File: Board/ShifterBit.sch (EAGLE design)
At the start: 14 parts, among them P1 PINHD-1X10, P2 PINHD-1X10

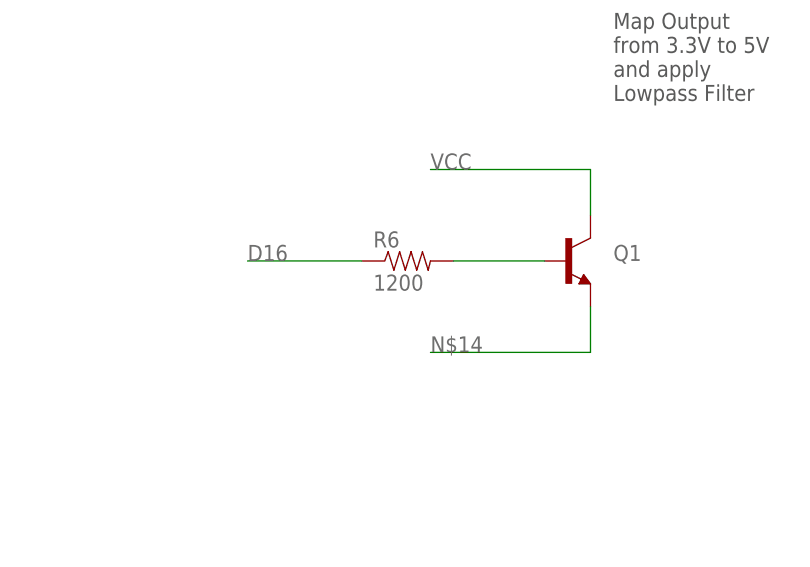
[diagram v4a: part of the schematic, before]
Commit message: changed resistor name
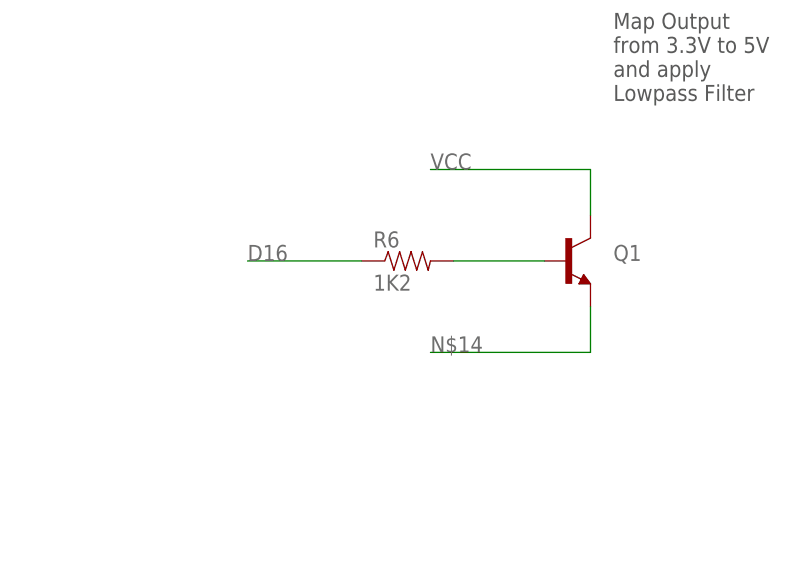
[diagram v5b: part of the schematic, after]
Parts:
- R6: value 1200 -> 1K2
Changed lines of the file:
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@@
 <part name="R5" library="SparkFun-Passives" deviceset="RESISTOR" device="0603-RES" value="560"/>
 <part name="Q1" library="SparkFun-DiscreteSemi" deviceset="TRANSISTOR_NPN" device="BC547"/>
-<part name="R6" library="SparkFun-Resistors" deviceset="RESISTOR" device="0603" value="1200"/>
+<part name="R6" library="SparkFun-Resistors" deviceset="RESISTOR" device="0603" value="1K2"/>
 </parts>
 <sheets>

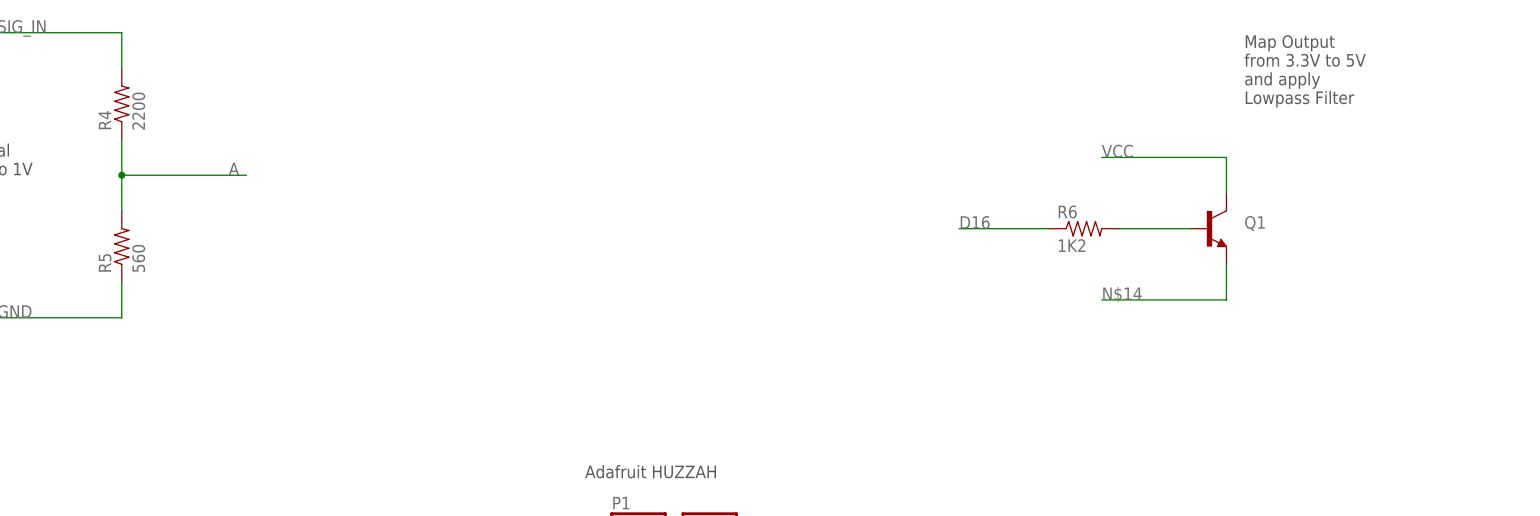
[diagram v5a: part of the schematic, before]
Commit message: added component to board
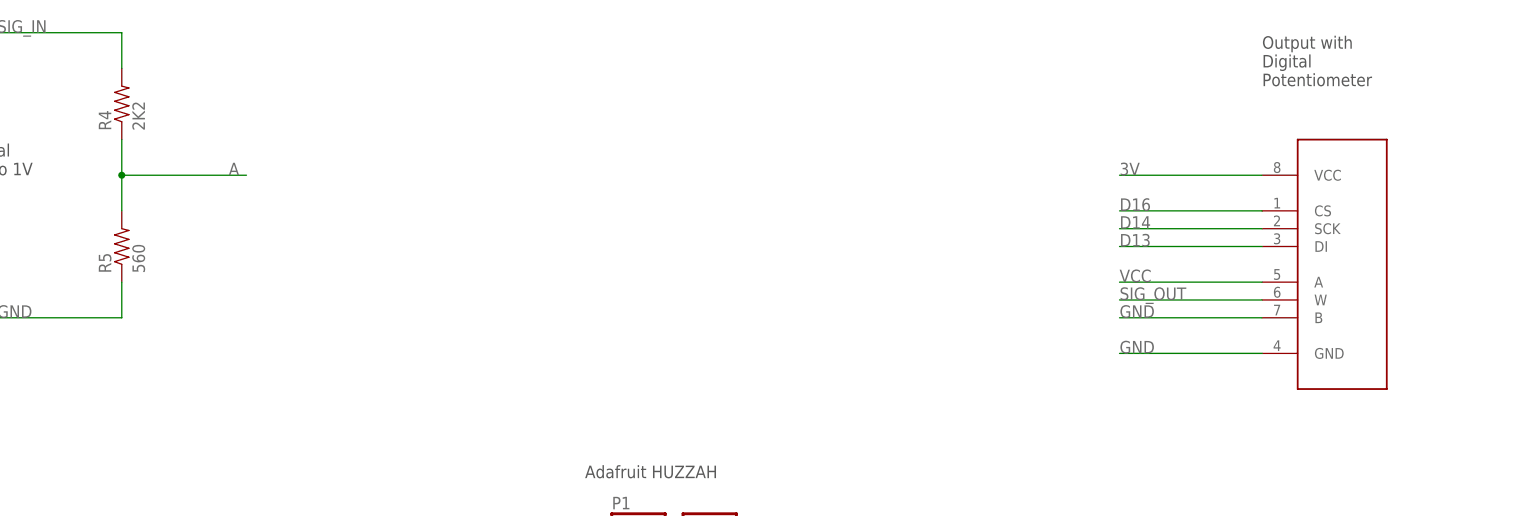
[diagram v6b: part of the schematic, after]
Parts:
- removed Q1: (no value), SparkFun-DiscreteSemi:TRANSISTOR_NPNBC547
- removed R6: 1K2, SparkFun-Resistors:RESISTOR0603
- added DPOT1: MCP41XXX, SparkFun-AnalogIC:MCP41XXX
- R4: value 2200 -> 2K2
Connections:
- removed net N$10: Q1.B, R6.2
- removed net N$14: Q1.E
- net 3V: now also DPOT1.VCC
- net D13: now also DPOT1.DI
- net D14: now also DPOT1.SCK
- net D16: now also DPOT1.CS; no longer R6.1
- net GND: now also DPOT1.B, DPOT1.GND
- net SIG_OUT: now also DPOT1.W
- net VCC: now also DPOT1.A; no longer Q1.C
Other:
- note added: "Output with Digital Potentiometer"
- note removed: "Map Output from 3.3V to 5V and apply Lowpass Filter"
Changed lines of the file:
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@@
 <layer number="56" name="wert" color="7" fill="1" visible="no" active="no"/>
 <layer number="57" name="tCAD" color="7" fill="1" visible="no" active="no"/>
+<layer number="59" name="tCarbon" color="7" fill="1" visible="no" active="no"/>
+<layer number="60" name="bCarbon" color="7" fill="1" visible="no" active="no"/>
 <layer number="90" name="Modules" color="5" fill="1" visible="yes" active="yes"/>
 <layer number="91" name="Nets" color="2" fill="1" visible="yes" active="yes"/>
@@
 <layer number="127" name="_tValues" color="7" fill="1" visible="yes" active="yes"/>
 <layer number="128" name="_bValues" color="7" fill="1" visible="yes" active="yes"/>
+<layer number="129" name="Mask" color="7" fill="1" visible="yes" active="yes"/>
 <layer number="131" name="tAdjust" color="7" fill="1" visible="yes" active="yes"/>
 <layer number="132" name="bAdjust" color="7" fill="1" visible="yes" active="yes"/>
@@
 <part name="R2" library="SparkFun-Passives" deviceset="RESISTOR" device="0603-RES" value="56"/>
 <part name="R3" library="SparkFun-Passives" deviceset="RESISTOR" device="0603-RES" value="56"/>
-<part name="R4" library="SparkFun-Passives" deviceset="RESISTOR" device="0603-RES" value="2200"/>
+<part name="R4" library="SparkFun-Passives" deviceset="RESISTOR" device="0603-RES" value="2K2"/>
 <part name="R5" library="SparkFun-Passives" deviceset="RESISTOR" device="0603-RES" value="560"/>
-<part name="Q1" library="SparkFun-DiscreteSemi" deviceset="TRANSISTOR_NPN" device="BC547"/>
-<part name="R6" library="SparkFun-Resistors" deviceset="RESISTOR" device="0603" value="1K2"/>
+<part name="DPOT1" library="SparkFun-AnalogIC" deviceset="MCP41XXX" device="" value="MCP41XXX"/>
 </parts>
 <sheets>
@@
 <text x="20.32" y="76.2" size="1.778" layer="97">Input</text>
 <text x="205.74" y="73.66" size="1.778" layer="97">Output</text>
-<text x="193.04" y="185.42" size="1.778" layer="97">Map Output
-from 3.3V to 5V
-and apply
-Lowpass Filter</text>
+<text x="195.58" y="187.96" size="1.778" layer="97">Output with
+Digital
+Potentiometer</text>
 </plain>
 <instances>
@@
 <instance part="R4" gate="G$1" x="33.02" y="185.42" rot="R90"/>
 <instance part="R5" gate="G$1" x="33.02" y="165.1" rot="R90"/>
-<instance part="Q1" gate="G$1" x="187.96" y="167.64"/>
-<instance part="R6" gate="G$1" x="170.18" y="167.64"/>
+<instance part="DPOT1" gate="G$1" x="205.74" y="154.94"/>
 </instances>
 <busses>
@@
 <label x="127" y="38.1" size="1.778" layer="95"/>
 </segment>
+<segment>
+<pinref part="DPOT1" gate="G$1" pin="GND"/>
+<wire x1="195.58" y1="149.86" x2="175.26" y2="149.86" width="0.1524" layer="91"/>
+<label x="175.26" y="149.86" size="1.778" layer="95"/>
+</segment>
+<segment>
+<pinref part="DPOT1" gate="G$1" pin="B"/>
+<wire x1="195.58" y1="154.94" x2="175.26" y2="154.94" width="0.1524" layer="91"/>
+<label x="175.26" y="154.94" size="1.778" layer="95"/>
+</segment>
 </net>
 <net name="VCC" class="0">
@@
 </segment>
 <segment>
-<pinref part="Q1" gate="G$1" pin="C"/>
-<wire x1="190.5" y1="172.72" x2="190.5" y2="177.8" width="0.1524" layer="91"/>
-<wire x1="190.5" y1="177.8" x2="172.72" y2="177.8" width="0.1524" layer="91"/>
-<label x="172.72" y="177.8" size="1.778" layer="95"/>
+<pinref part="DPOT1" gate="G$1" pin="A"/>
+<wire x1="195.58" y1="160.02" x2="175.26" y2="160.02" width="0.1524" layer="91"/>
+<label x="175.26" y="160.02" size="1.778" layer="95"/>
 </segment>
 </net>
@@
 <wire x1="215.9" y1="63.5" x2="195.58" y2="63.5" width="0.1524" layer="91"/>
 <label x="195.58" y="63.5" size="1.778" layer="95"/>
+</segment>
+<segment>
+<pinref part="DPOT1" gate="G$1" pin="W"/>
+<wire x1="195.58" y1="157.48" x2="175.26" y2="157.48" width="0.1524" layer="91"/>
+<label x="175.26" y="157.48" size="1.778" layer="95"/>
 </segment>
 </net>
@@
 </segment>
 <segment>
-<pinref part="R6" gate="G$1" pin="1"/>
-<wire x1="165.1" y1="167.64" x2="152.4" y2="167.64" width="0.1524" layer="91"/>
-<label x="152.4" y="167.64" size="1.778" layer="95"/>
+<pinref part="DPOT1" gate="G$1" pin="CS"/>
+<wire x1="195.58" y1="170.18" x2="175.26" y2="170.18" width="0.1524" layer="91"/>
+<label x="175.26" y="170.18" size="1.778" layer="95"/>
 </segment>
 </net>
@@
 <label x="127" y="40.64" size="1.778" layer="95"/>
 </segment>
+<segment>
+<pinref part="DPOT1" gate="G$1" pin="SCK"/>
+<wire x1="195.58" y1="167.64" x2="175.26" y2="167.64" width="0.1524" layer="91"/>
+<label x="175.26" y="167.64" size="1.778" layer="95"/>
+</segment>
 </net>
 <net name="D12" class="0">
@@
 <label x="127" y="45.72" size="1.778" layer="95"/>
 </segment>
+<segment>
+<pinref part="DPOT1" gate="G$1" pin="DI"/>
+<wire x1="195.58" y1="165.1" x2="175.26" y2="165.1" width="0.1524" layer="91"/>
+<label x="175.26" y="165.1" size="1.778" layer="95"/>
+</segment>
 </net>
 <net name="V+" class="0">
@@
 <label x="127" y="43.18" size="1.778" layer="95"/>
 </segment>
+<segment>
+<pinref part="DPOT1" gate="G$1" pin="VCC"/>
+<wire x1="195.58" y1="175.26" x2="175.26" y2="175.26" width="0.1524" layer="91"/>
+<label x="175.26" y="175.26" size="1.778" layer="95"/>
+</segment>
 </net>
 <net name="LD0" class="0">
@@
 </segment>
 </net>
-<net name="N$14" class="0">
-<segment>
-<pinref part="Q1" gate="G$1" pin="E"/>
-<wire x1="190.5" y1="162.56" x2="190.5" y2="157.48" width="0.1524" layer="91"/>
-<wire x1="190.5" y1="157.48" x2="172.72" y2="157.48" width="0.1524" layer="91"/>
-<label x="172.72" y="157.48" size="1.778" layer="95"/>
-</segment>
-</net>
-<net name="N$10" class="0">
-<segment>
-<pinref part="R6" gate="G$1" pin="2"/>
-<pinref part="Q1" gate="G$1" pin="B"/>
-<wire x1="175.26" y1="167.64" x2="185.42" y2="167.64" width="0.1524" layer="91"/>
-</segment>
-</net>

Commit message: added some aesthetics
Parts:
- R4: value 2K2 -> 3K3
- R5: value 560 -> 820
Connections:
- net 3V: no longer DPOT1.VCC
- net VCC: now also DPOT1.VCC
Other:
- note added: "Map input signal from 5V to 1V"
- note removed: "Map Signal from 5V to 1V"
- moved on the sheet: BSF1, BSM1, LED1, LED2, P1, P2, R1, R2, R3, R4, R5, SD1

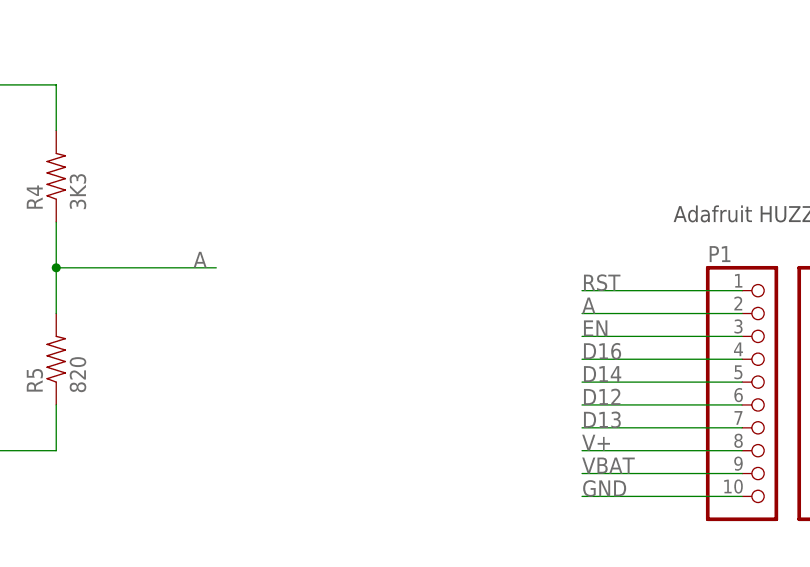
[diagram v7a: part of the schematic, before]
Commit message: renamed signal
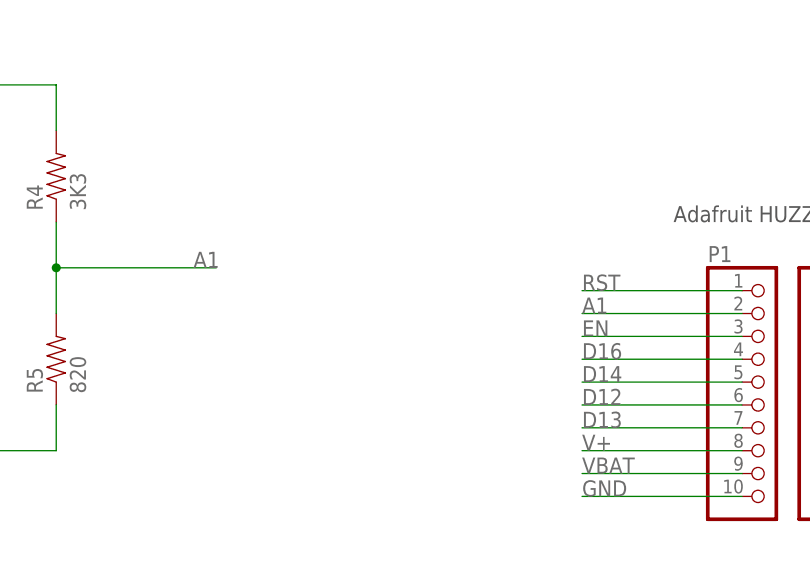
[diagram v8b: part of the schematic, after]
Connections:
- net A renamed A1
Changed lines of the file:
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@@
 </segment>
 </net>
-<net name="A" class="0">
+<net name="A1" class="0">
 <segment>
 <pinref part="P1" gate="G$1" pin="2"/>
